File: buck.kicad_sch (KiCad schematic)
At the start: 20 parts, among them IC1 RT6285GSP, IC2 LV2862YDDCR

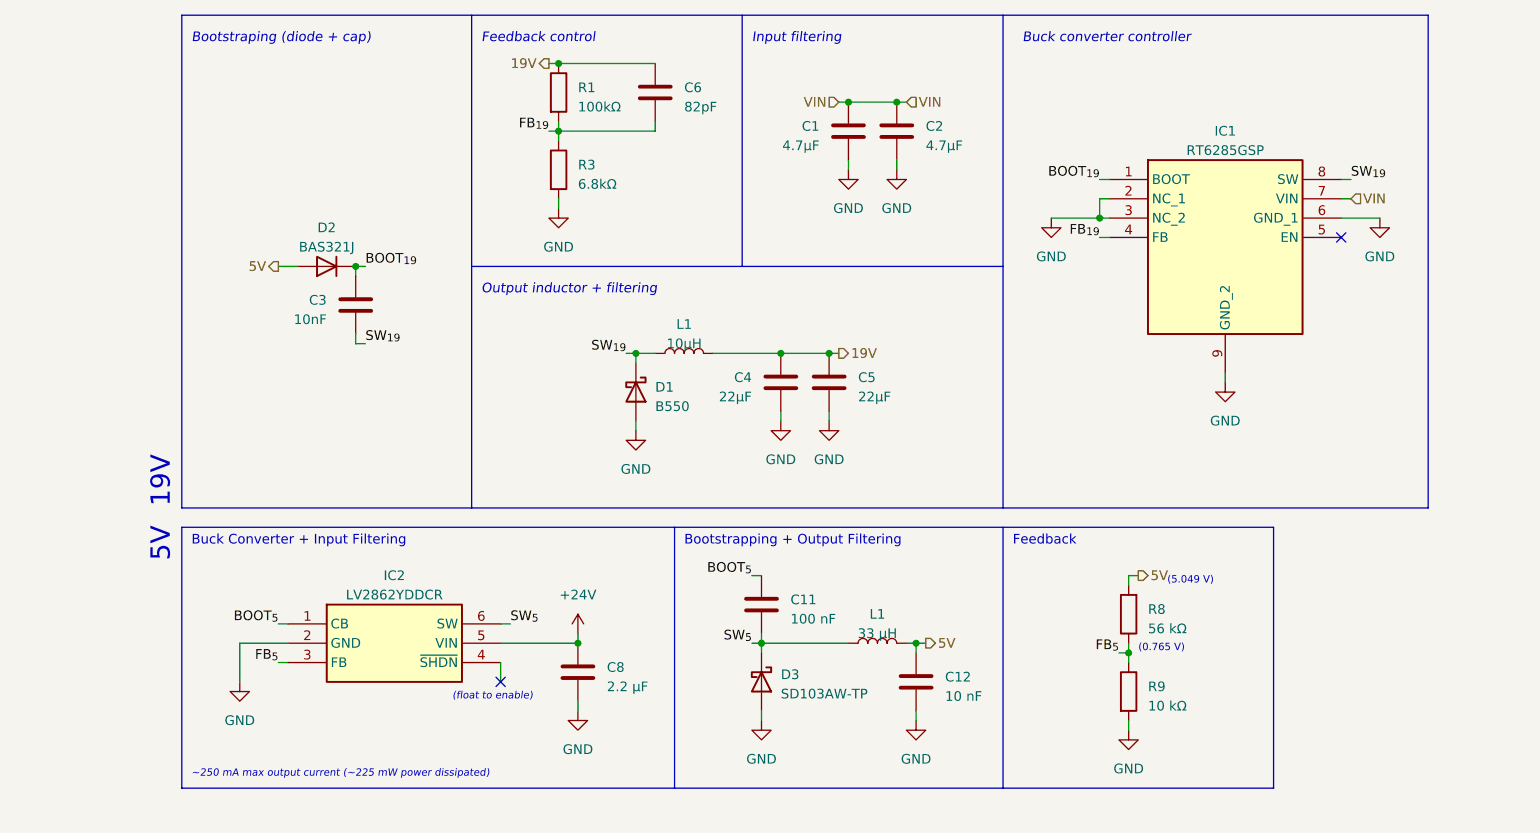
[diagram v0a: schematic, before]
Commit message: Added test points + part number for diode
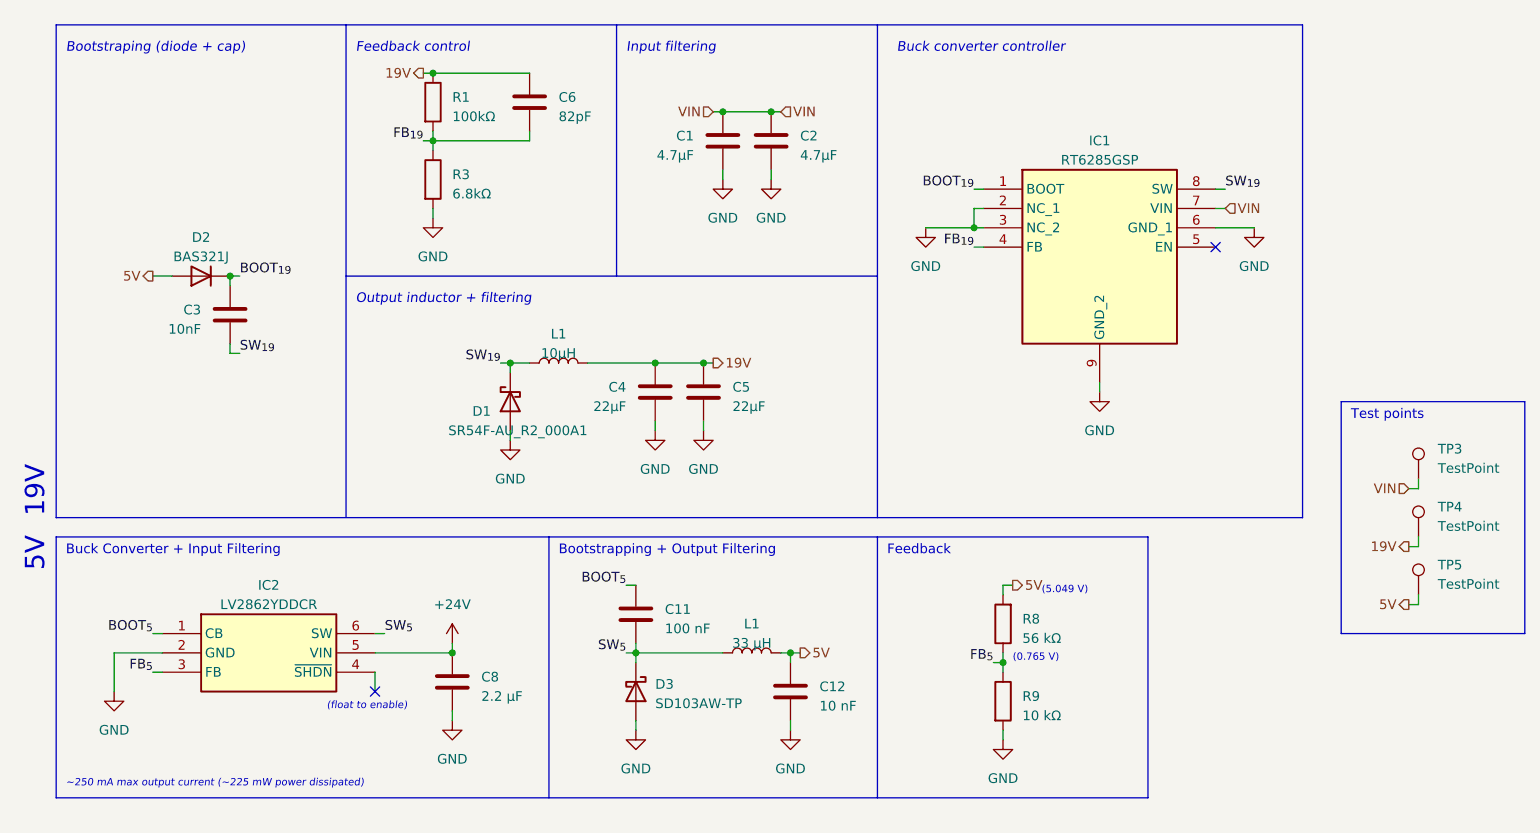
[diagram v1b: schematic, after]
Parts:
- added TP3, TP4, TP5: TestPoint, TestPoint:TestPoint_Pad_2.0x2.0mm, symbol Connector:TestPoint
- D1: value B550 -> SR54F-AU_R2_000A1
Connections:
- net 19V: now also TP4.1
- net 5V: now also TP5.1
- net VIN: now also TP3.1
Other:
- note added: "Test points"
- moved on the sheet: C1, C11, C12, C2, C3, C4, C5, C6, C8, D1, D2, D3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

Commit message: Lots of placements
Big blocks done, time to shuffle them around until I'm happy + route them
4-layer board in the future?
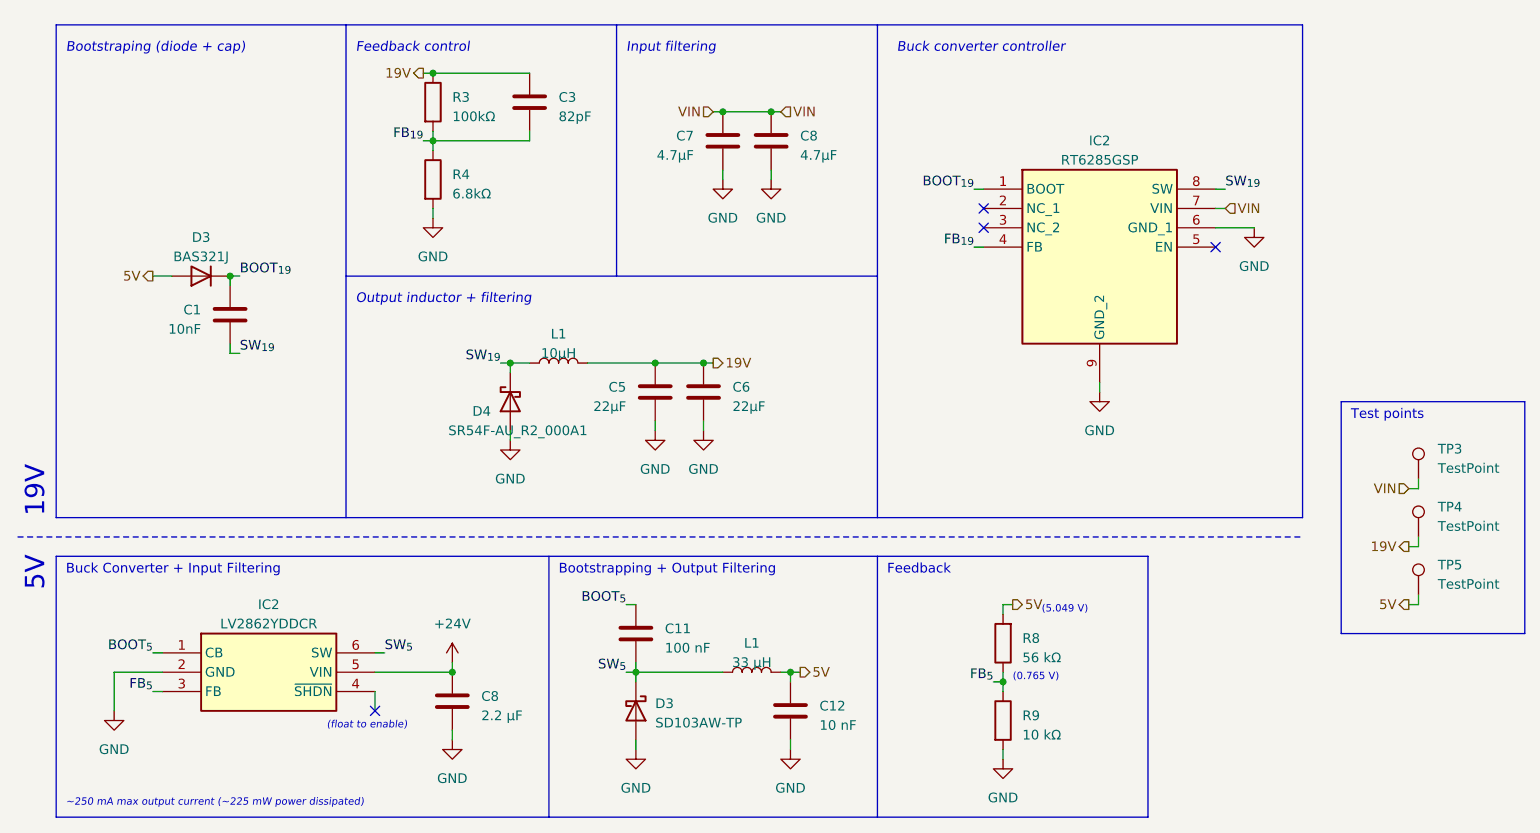
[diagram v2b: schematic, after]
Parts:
- renumbered C3 to C1, C6 to C3, C4 to C5, C5 to C6, C1 to C7, C2 to C8, D2 to D3, D1 to D4, IC1 to IC2, R1 to R3, R3 to R4
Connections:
- net GND: no longer IC2.2 (NC_1), IC2.3 (NC_2)
- no-connect marks 2 -> 4
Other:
- moved on the sheet: C11, C12, C8, D3, IC2, L1, R8, R9

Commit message: Finished routing
Turns out we don't need the +5V buck kek
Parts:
- C5, C6: footprint Capacitor_SMD:C_0805_2012Metric_Pad1.18x1.45mm_HandSolder -> Capacitor_SMD:C_0603_1608Metric_Pad1.08x0.95mm_HandSolder
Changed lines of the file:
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@@
       (effects (font (size 1.27 1.27)) (justify left))
     )
-    (property "Footprint" "Capacitor_SMD:C_0805_2012Metric_Pad1.18x1.45mm_HandSolder" (at 126.0348 97.79 0)
+    (property "Footprint" "Capacitor_SMD:C_0603_1608Metric_Pad1.08x0.95mm_HandSolder" (at 126.0348 97.79 0)
       (effects (font (size 1.27 1.27)) hide)
     )
@@
       (effects (font (size 1.27 1.27)) (justify left))
     )
-    (property "Footprint" "Capacitor_SMD:C_0805_2012Metric_Pad1.18x1.45mm_HandSolder" (at 134.3152 97.79 0)
+    (property "Footprint" "Capacitor_SMD:C_0603_1608Metric_Pad1.08x0.95mm_HandSolder" (at 134.3152 97.79 0)
       (effects (font (size 1.27 1.27)) hide)
     )

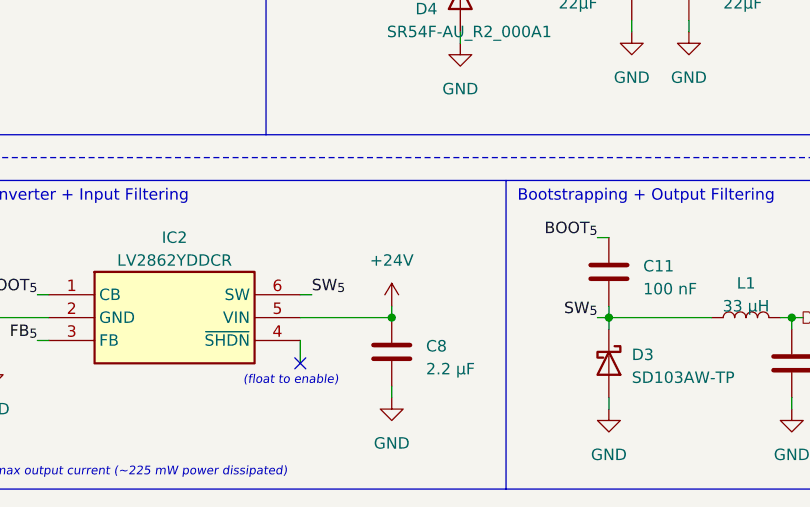
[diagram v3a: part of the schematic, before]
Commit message: Touched up everything
Improved pours + thermal pads, better routing, trace length matching
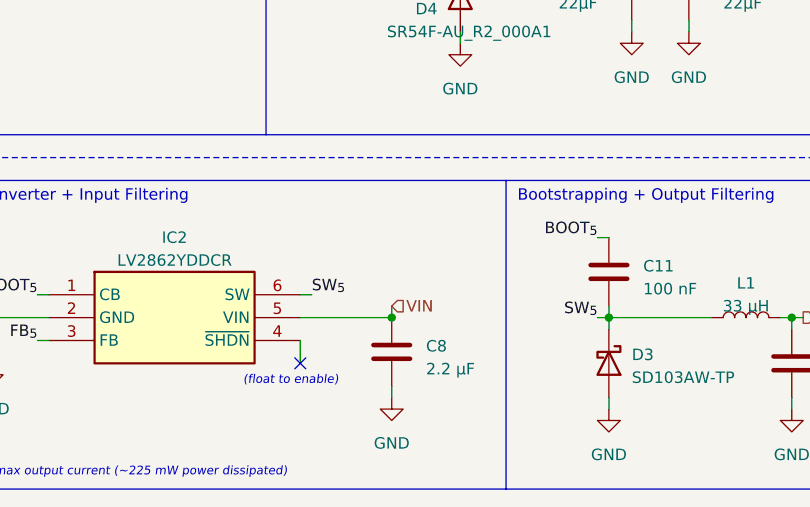
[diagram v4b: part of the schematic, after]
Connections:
- net +24V is gone; now on net VIN: C8.1, IC2.5 (VIN)
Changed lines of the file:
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@@
+    (effects (font (size 1.27 1.27)) (justify left))
+  )
+  (hierarchical_label "VIN" (shape input) (at 100.33 129.54 0) (fields_autoplaced)
     (effects (font (size 1.27 1.27)) (justify left))
   )
@@
         )
       )
-    )
-  )
-  (symbol (lib_id "power:+24V") (at 100.33 129.54 0) (unit 1)
-    (in_bom yes) (on_board yes) (dnp no) (fields_autoplaced)
-    (property "Reference" "#PWR0164" (at 100.33 133.35 0)
-      (effects (font (size 1.27 1.27)) hide)
-    )
-    (property "Value" "+24V" (at 100.33 124.46 0)
-      (effects (font (size 1.27 1.27)))
-    )
-    (property "Footprint" "" (at 100.33 129.54 0)
-      (effects (font (size 1.27 1.27)) hide)
-    )
-    (property "Datasheet" "" (at 100.33 129.54 0)
-      (effects (font (size 1.27 1.27)) hide)
-    )
-    (pin "1")
-    (instances
-      (project "VehicleControlUnit"
-        (path "/266714a0-d820-41e6-8c76-c78ad7e99270/e39c3e54-ebea-4544-a480-db7410a9de4a"
-          (reference "#PWR0164") (unit 1)
-        )
-      )
-      (project "power_converion_23_saved"
-        (path "/2b458daa-d7b0-4b90-833f-0b221fa8afe2"
-          (reference "#PWR01") (unit 1)
-        )
-      )
-      (project "UnsprungDynamicsModule"
-        (path "/7466de43-27f3-4538-bb02-85a2b212d799/e9ecdafa-e73e-4017-98f5-a93e16b4c821"
-          (reference "#PWR034") (unit 1)
-        )
-      )
-      (project "Chassis"
-        (path "/d5f28ba3-2393-441a-9a3a-5aa9d797472a/632f64e1-f4ac-4fce-8dc1-2a6086852be0"
-          (reference "#PWR021") (unit 1)
-        )
-      )

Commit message: Create new STEP files
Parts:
- added R11: 100kΩ, Resistor_SMD:R_0603_1608Metric_Pad0.98x0.95mm_HandSolder, symbol Device:R_Small
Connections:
- net VIN: now also R11.2
- net ~{SHDN}: now reaches IC2.4 (~{SHDN})
- net ~{SHDN}: now also R11.1
- no-connect marks 4 -> 3
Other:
- note removed: "(float to enable)"
- note removed: "~250 mA max output current (~225 mW power dissipated)"
- moved on the sheet: C8
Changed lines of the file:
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@@
     (company "UT RoboMasters")
   )
+  (junction (at 91.44 133.35) (diameter 0) (color 0 0 0 0)
+  )
   (junction (at 100.33 130.81) (diameter 0) (color 0 0 0 0)
   )
@@
   (junction (at 135.89 57.15) (diameter 0) (color 0 0 0 0)
   )
+  (junction (at 100.33 133.35) (diameter 0) (color 0 0 0 0)
+  )
   (junction (at 97.79 60.96) (diameter 0) (color 0 0 0 0)
   )
@@
   )
   (no_connect (at 170.18 69.85))
-  (no_connect (at 90.17 135.89))
   (no_connect (at 200.66 74.93))
   (no_connect (at 170.18 72.39))
@@
     (stroke (width 0) (type default))
   )
-  (wire (pts (xy 90.17 135.89) (xy 90.17 133.35))
+  (wire (pts (xy 102.87 130.81) (xy 100.33 130.81))
     (stroke (width 0) (type default))
   )
@@
   )
   (wire (pts (xy 124.46 129.54) (xy 124.46 130.81))
+    (stroke (width 0) (type default))
+  )
+  (wire (pts (xy 91.44 134.62) (xy 91.44 133.35))
     (stroke (width 0) (type default))
   )
@@
     (stroke (width 0) (type dash))
   )
-  (wire (pts (xy 100.33 138.43) (xy 100.33 139.7))
+  (wire (pts (xy 100.33 142.24) (xy 100.33 143.51))
     (stroke (width 0) (type default))
   )
@@
     (stroke (width 0) (type default))
   )
+  (wire (pts (xy 97.79 133.35) (xy 100.33 133.35))
+    (stroke (width 0) (type default))
+  )
+  (wire (pts (xy 100.33 133.35) (xy 100.33 130.81))
+    (stroke (width 0) (type default))
+  )
   (polyline (pts (xy 86.36 78.74) (xy 156.21 78.74))
     (stroke (width 0) (type default))
   )
+  (wire (pts (xy 90.17 133.35) (xy 91.44 133.35))
+    (stroke (width 0) (type default))
+  )
   (wire (pts (xy 133.35 97.79) (xy 133.35 99.06))
     (stroke (width 0) (type default))
@@
     (stroke (width 0) (type default))
   )
-  (wire (pts (xy 100.33 129.54) (xy 100.33 130.81))
+  (wire (pts (xy 100.33 134.62) (xy 100.33 133.35))
     (stroke (width 0) (type default))
   )
@@
     (stroke (width 0) (type default))
   )
+  (wire (pts (xy 91.44 133.35) (xy 92.71 133.35))
+    (stroke (width 0) (type default))
+  )
   (wire (pts (xy 123.19 121.92) (xy 124.46 121.92))
     (stroke (width 0) (type default))
@@
   (wire (pts (xy 144.78 130.81) (xy 146.05 130.81))
     (stroke (width 0) (type default))
-  )
-  (text "(float to enable)" (at 83.82 138.43 0)
-    (effects (font (size 0.96 0.96) italic) (justify left bottom))
   )
   (text "Buck converter controller" (at 158.75 49.53 0)
@@
     (effects (font (size 1.27 1.27)) (justify left bottom))
   )
-  (text "~250 mA max output current (~225 mW power dissipated)"
-    (at 49.53 148.59 0)
-    (effects (font (size 0.96 0.96) italic) (justify left bottom))
-  )
   (label "BOOT_{5}" (at 123.19 121.92 180) (fields_autoplaced)
     (effects (font (size 1.27 1.27)) (justify right bottom))
   )
+  (label "~{SHDN}" (at 91.44 134.62 270) (fields_autoplaced)
+    (effects (font (size 0.762 0.762)) (justify right bottom))
+  )
   (label "BOOT_{19}" (at 168.91 67.31 180) (fields_autoplaced)
     (effects (font (size 1.27 1.27)) (justify right bottom))
@@
     (effects (font (size 1.27 1.27)) (justify left))
   )
-  (hierarchical_label "VIN" (shape input) (at 100.33 129.54 0) (fields_autoplaced)
+  (hierarchical_label "VIN" (shape input) (at 102.87 130.81 0) (fields_autoplaced)
     (effects (font (size 1.27 1.27)) (justify left))
   )
@@
     )
   )
-  (symbol (lib_id "Device:C") (at 100.33 134.62 0) (unit 1)
+  (symbol (lib_id "Device:C") (at 100.33 138.43 0) (unit 1)
     (in_bom yes) (on_board yes) (dnp no)
-    (property "Reference" "C8" (at 104.14 133.985 0)
-      (effects (font (size 1.27 1.27)) (justify left))
-    )
-    (property "Value" "2.2 μF" (at 104.14 136.525 0)
-      (effects (font (size 1.27 1.27)) (justify left))
-    )
-    (property "Footprint" "Capacitor_SMD:C_0603_1608Metric_Pad1.08x0.95mm_HandSolder" (at 101.2952 138.43 0)
-      (effects (font (size 1.27 1.27)) hide)
-    )
-    (property "Datasheet" "https://www.mouser.com/datasheet/2/585/MLCC-1837944.pdf" (at 100.33 134.62 0)
+    (property "Reference" "C8" (at 104.14 137.795 0)
+      (effects (font (size 1.27 1.27)) (justify left))
+    )
+    (property "Value" "2.2 μF" (at 104.14 140.335 0)
+      (effects (font (size 1.27 1.27)) (justify left))
+    )
+    (property "Footprint" "Capacitor_SMD:C_0603_1608Metric_Pad1.08x0.95mm_HandSolder" (at 101.2952 142.24 0)
+      (effects (font (size 1.27 1.27)) hide)
+    )
+    (property "Datasheet" "https://www.mouser.com/datasheet/2/585/MLCC-1837944.pdf" (at 100.33 138.43 0)
       (effects (font (size 1.27 1.27)) hide)
     )
@@
     )
   )
-  (symbol (lib_id "power:GND") (at 100.33 139.7 0) (unit 1)
-    (in_bom yes) (on_board yes) (dnp no) (fields_autoplaced)
-    (property "Reference" "#PWR035" (at 100.33 146.05 0)
-      (effects (font (size 1.27 1.27)) hide)
-    )
-    (property "Value" "GND" (at 100.33 144.78 0)
-      (effects (font (size 1.27 1.27)))
-    )
-    (property "Footprint" "" (at 100.33 139.7 0)
-      (effects (font (size 1.27 1.27)) hide)
-    )
-    (property "Datasheet" "" (at 100.33 139.7 0)
-      (effects (font (size 1.27 1.27)) hide)
-    )
+  (symbol (lib_id "Device:R_Small") (at 95.25 133.35 90) (mirror x) (unit 1)
+    (in_bom yes) (on_board yes) (dnp no)
+    (property "Reference" "R11" (at 95.25 138.43 90)
+      (effects (font (size 1.27 1.27)))
+    )
+    (property "Value" "100kΩ" (at 95.25 135.89 90)
+      (effects (font (size 1.27 1.27)))
+    )
+    (property "Footprint" "Resistor_SMD:R_0603_1608Metric_Pad0.98x0.95mm_HandSolder" (at 95.25 133.35 0)
+      (effects (font (size 1.27 1.27)) hide)
+    )
+    (property "Datasheet" "~" (at 95.25 133.35 0)
+      (effects (font (size 1.27 1.27)) hide)
+    )
+    (pin "1")
+    (pin "2")
+    (instances
+      (project "Chassis"
+        (path "/d5f28ba3-2393-441a-9a3a-5aa9d797472a/632f64e1-f4ac-4fce-8dc1-2a6086852be0"
+          (reference "R11") (unit 1)
+        )
+      )
+    )
+  )
+  (symbol (lib_id "power:GND") (at 100.33 143.51 0) (unit 1)
+    (in_bom yes) (on_board yes) (dnp no) (fields_autoplaced)
+    (property "Reference" "#PWR035" (at 100.33 149.86 0)
+      (effects (font (size 1.27 1.27)) hide)
+    )
+    (property "Value" "GND" (at 100.33 148.59 0)
+      (effects (font (size 1.27 1.27)))
+    )
+    (property "Footprint" "" (at 100.33 143.51 0)
+      (effects (font (size 1.27 1.27)) hide)
+    )
+    (property "Datasheet" "" (at 100.33 143.51 0)
+      (effects (font (size 1.27 1.27)) hide)
+    )

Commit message: Update libraries & changed footprints
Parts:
- D4: footprint Robomaster_ICs:SODFL5336X110N -> Robomaster_Passives:SODFL5336X110N
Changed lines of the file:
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@@
       (effects (font (size 1.27 1.27)) (justify left))
     )
-    (property "Footprint" "Robomaster_ICs:SODFL5336X110N" (at 107.95 95.25 0)
+    (property "Footprint" "Robomaster_Passives:SODFL5336X110N" (at 107.95 95.25 0)
       (effects (font (size 1.27 1.27)) hide)
     )
